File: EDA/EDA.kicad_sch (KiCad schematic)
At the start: 38 parts, among them J2 Screw_Terminal_01x02, M1 Motor_Servo, U1 PMCF8316A1VRGFR, U2 LM2596S-5, U3 LM2678S-5

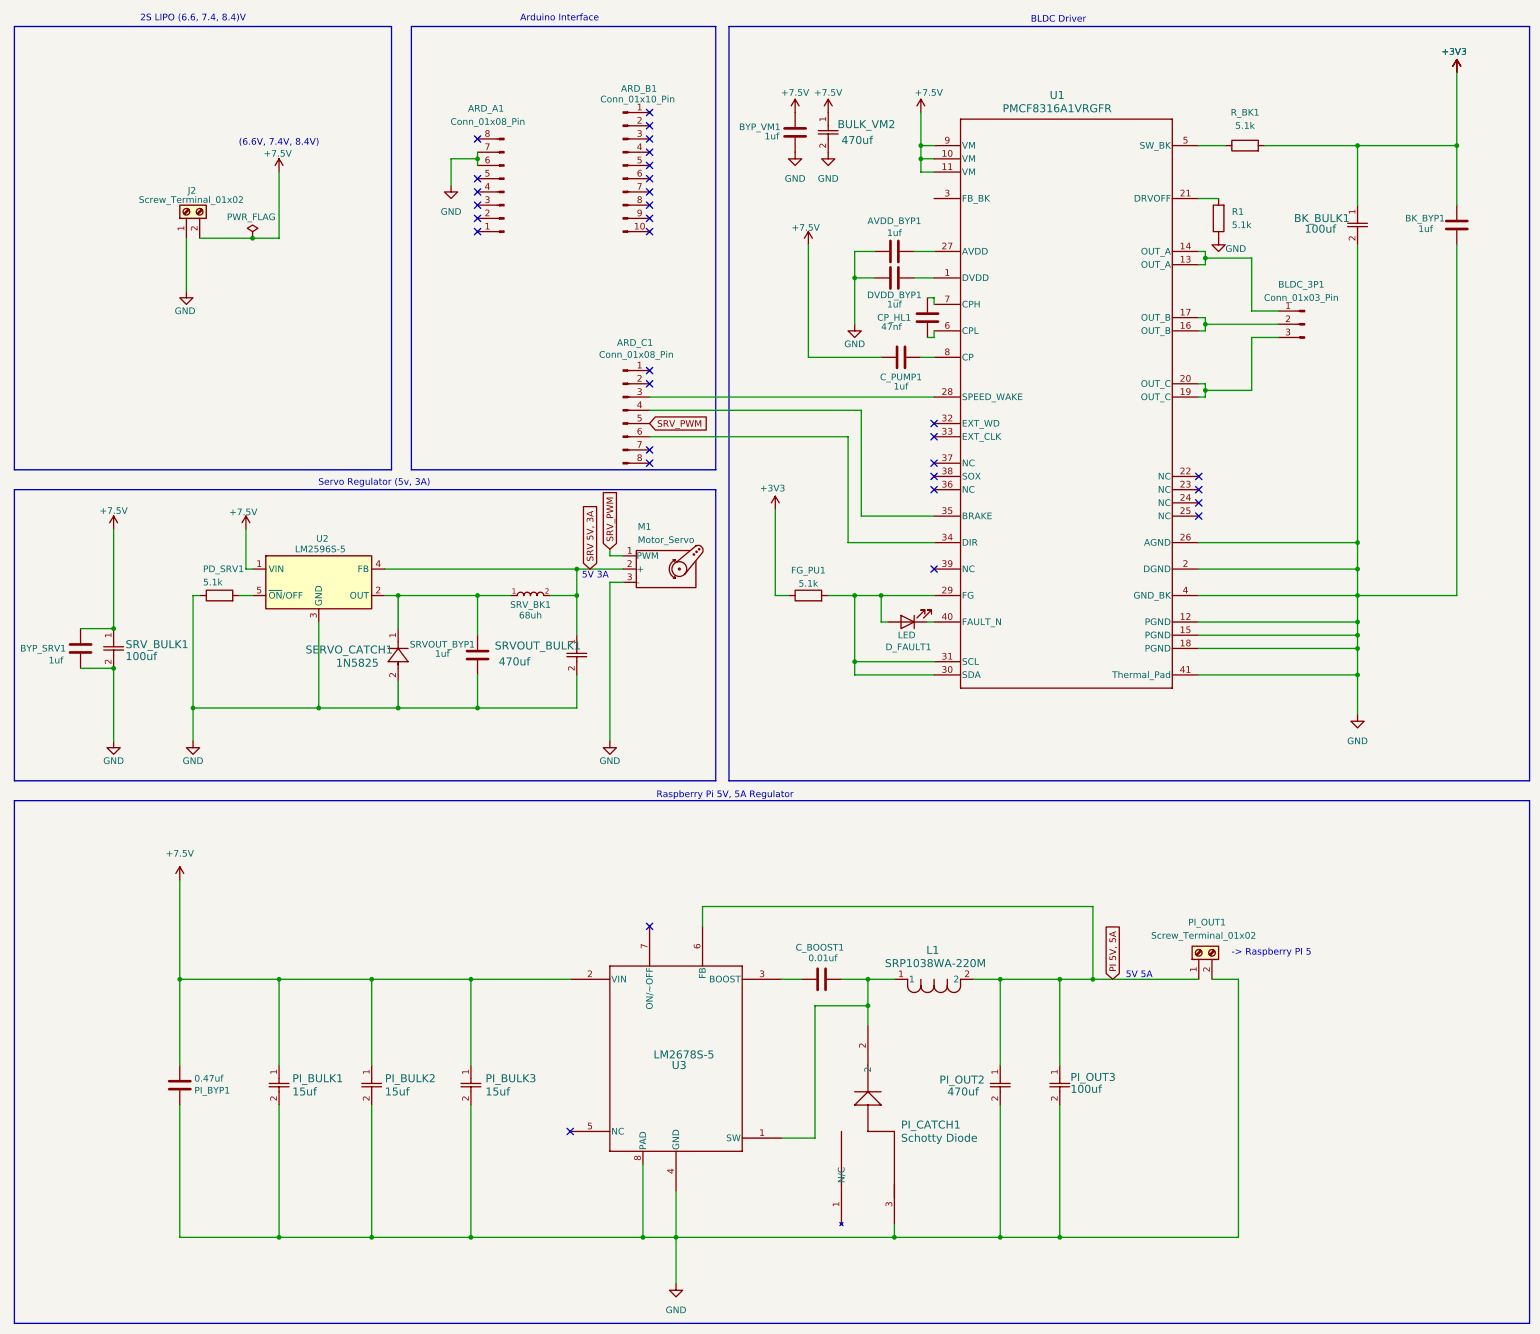
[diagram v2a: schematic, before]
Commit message: Add footprints for RGF0040E and LM2678S-12 components and update documentation
- Created new footprint files for RGF0040E-IPC_C and RGF0040E-MFG in KiCAD format.
- Created a new symbol for the LM2678S-12 in the KiCAD symbol library.
- Added three footprints (TS7B, TS7B-L, TS7B-M) for the LM2678S-12 in the KiCAD footprint library.
- Established a project plan document outlining milestones and tasks for upcoming development phases.
- Each footprint includes detailed pad and line definitions, along with silk screen and courtyard outlines.
- Updated properties for reference, value, and datasheet links in the symbol and footprints.
- Refactor schematic for clarity and readablity.
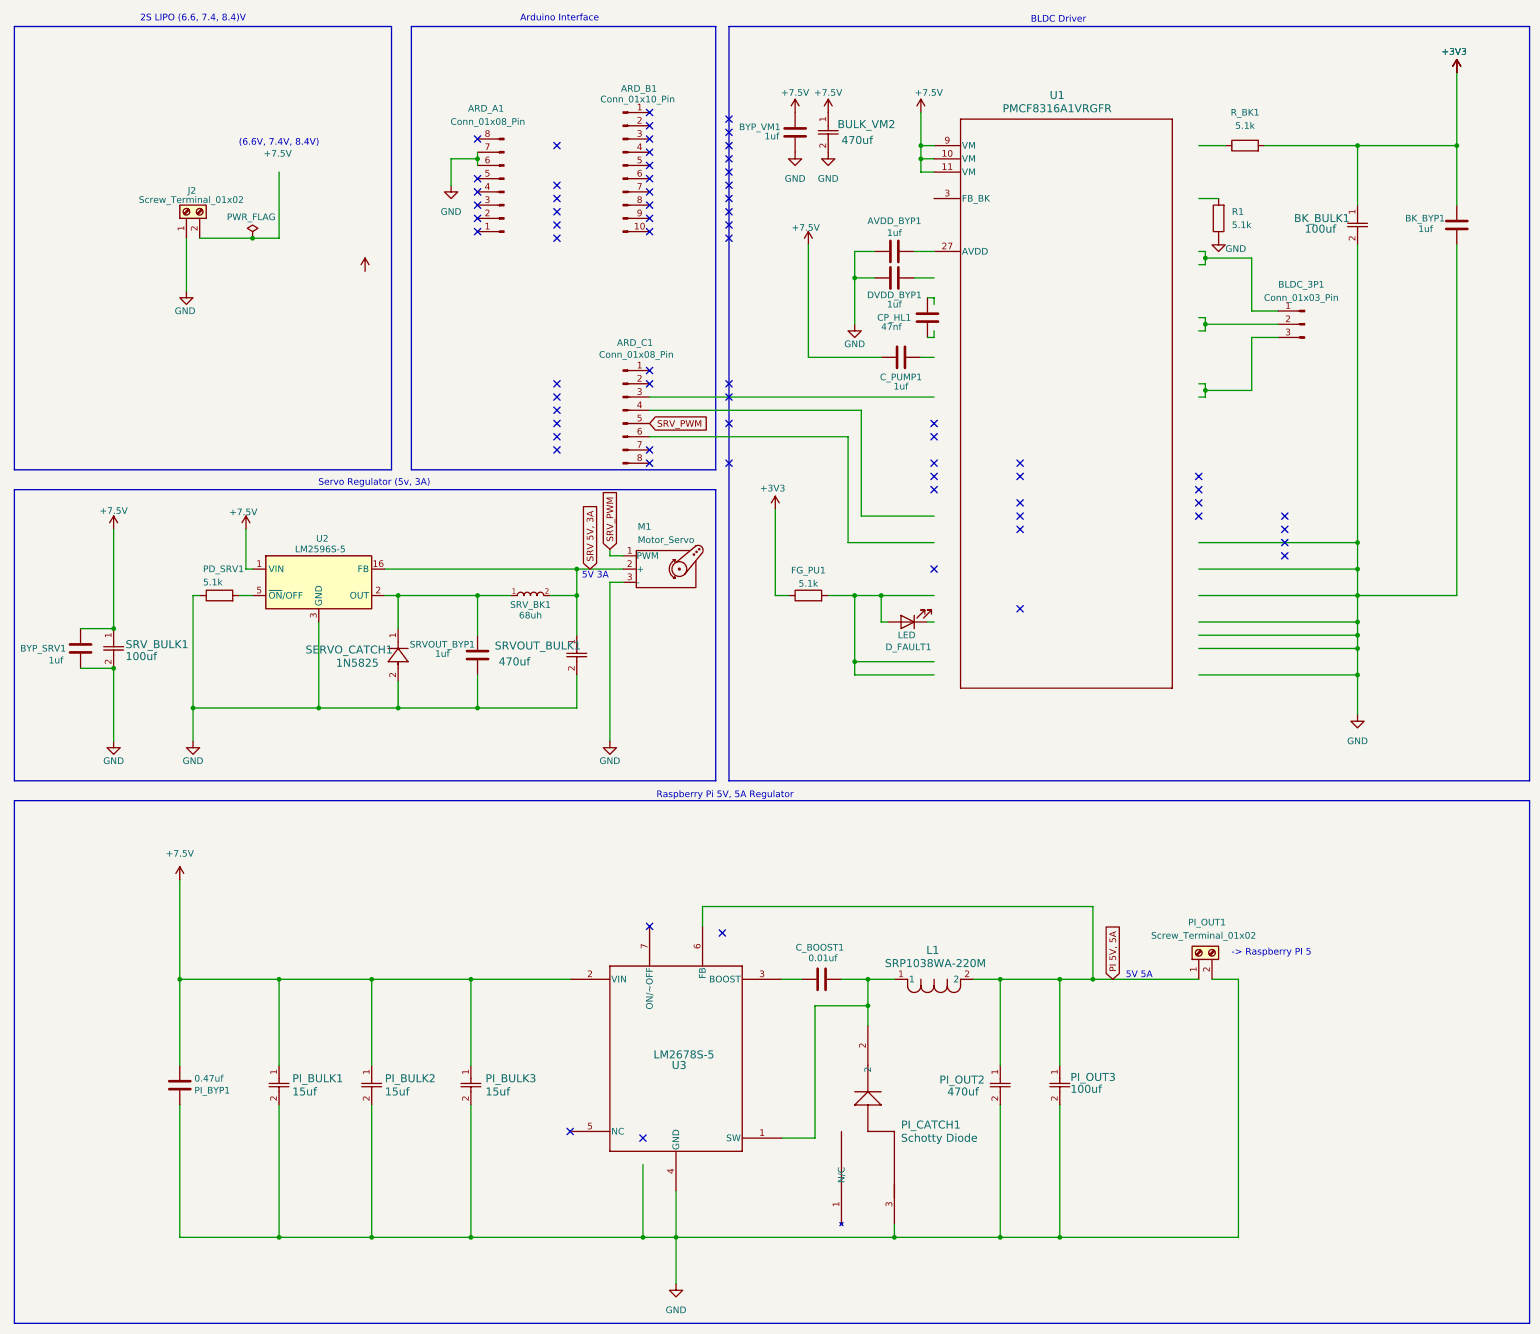
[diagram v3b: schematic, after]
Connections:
- net +7.5V: no longer J2.2 (Pin_2)
- net GND: no longer U1.12 (PGND), U1.15 (PGND), U1.18 (PGND), U1.2 (DGND), U1.26 (AGND), U1.4 (GND_BK), U1.41 (Thermal_Pad), U3.8 (PAD)
- net SRV 5V, 3A: now also U2.16 (FB); no longer U2.4 (FB)
- net at R_BK1.1: no longer U1.5 (SW_BK)
- net at ARD_C1.3 (Pin_3): no longer U1.28 (SPEED_WAKE)
- net at ARD_C1.4 (Pin_4): no longer U1.35 (BRAKE)
- net at ARD_C1.6 (Pin_6): no longer U1.34 (DIR)
- net at DVDD_BYP1.1: no longer U1.1 (DVDD)
- net at R1.2: no longer U1.21 (DRVOFF)
- net at D_FAULT1.1 (K): no longer U1.40 (FAULT_N)
- net at CP_HL1.2: no longer U1.6 (CPL)
- net at CP_HL1.1: no longer U1.7 (CPH)
- net at C_PUMP1.2: no longer U1.8 (CP)
- new net: D_FAULT1.2 (A), FG_PU1.2
- now unconnected: BLDC_3P1.1 (Pin_1), BLDC_3P1.2 (Pin_2), BLDC_3P1.3 (Pin_3)
- no-connect marks 32 -> 70
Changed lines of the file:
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@@
 		(at 105.41 38.1)
 	)
+	(no_connect
+		(at 153.67 41.91)
+	)
+	(no_connect
+		(at 260.35 115.57)
+	)
+	(no_connect
+		(at 152.4 190.5)
+	)
+	(no_connect
+		(at 153.67 34.29)
+	)
+	(no_connect
+		(at 209.55 113.03)
+	)
+	(no_connect
+		(at 209.55 102.87)
+	)
+	(no_connect
+		(at 153.67 49.53)
+	)
+	(no_connect
+		(at 153.67 39.37)
+	)
+	(no_connect
+		(at 120.65 52.07)
+	)
+	(no_connect
+		(at 137.16 229.87)
+	)
+	(no_connect
+		(at 153.67 87.63)
+	)
+	(no_connect
+		(at 209.55 128.27)
+	)
+	(no_connect
+		(at 120.65 87.63)
+	)
+	(no_connect
+		(at 120.65 95.25)
+	)
+	(no_connect
+		(at 153.67 85.09)
+	)
+	(no_connect
+		(at 120.65 97.79)
+	)
+	(no_connect
+		(at 153.67 100.33)
+	)
+	(no_connect
+		(at 260.35 118.11)
+	)
+	(no_connect
+		(at 120.65 46.99)
+	)
+	(no_connect
+		(at 153.67 54.61)
+	)
+	(no_connect
+		(at 153.67 36.83)
+	)
+	(no_connect
+		(at 153.67 44.45)
+	)
+	(no_connect
+		(at 260.35 110.49)
+	)
+	(no_connect
+		(at 120.65 57.15)
+	)
+	(no_connect
+		(at 153.67 46.99)
+	)
+	(no_connect
+		(at 120.65 49.53)
+	)
+	(no_connect
+		(at 209.55 100.33)
+	)
+	(no_connect
+		(at 153.67 52.07)
+	)
+	(no_connect
+		(at 209.55 110.49)
+	)
+	(no_connect
+		(at 120.65 39.37)
+	)
+	(no_connect
+		(at 120.65 54.61)
+	)
+	(no_connect
+		(at 120.65 92.71)
+	)
+	(no_connect
+		(at 120.65 90.17)
+	)
+	(no_connect
+		(at 120.65 85.09)
+	)
+	(no_connect
+		(at 153.67 92.71)
+	)
+	(no_connect
+		(at 153.67 57.15)
+	)
+	(no_connect
+		(at 260.35 113.03)
+	)
+	(no_connect
+		(at 209.55 107.95)
+	)
 	(wire
 		(pts
@@
 	(symbol
 		(lib_id "power:+7.5V")
-		(at 67.31 44.45 0)
+		(at 83.82 63.5 0)
 		(unit 1)
 		(exclude_from_sim no)
@@
 		(dnp no)
 		(property "Reference" "#PWR01"
-			(at 67.31 48.26 0)
+			(at 83.82 67.31 0)
 			(effects
 				(font
@@
 		)
 		(property "Footprint" ""
-			(at 67.31 44.45 0)
+			(at 83.82 63.5 0)
 			(effects
 				(font
@@
 		)
 		(property "Datasheet" ""
-			(at 67.31 44.45 0)
+			(at 83.82 63.5 0)
 			(effects
 				(font
@@
 		)
 		(property "Description" "Power symbol creates a global label with name \"+7.5V\""
-			(at 67.31 44.45 0)
+			(at 83.82 63.5 0)
 			(effects
 				(font
@@
 				(font
 					(size 1.27 1.27)
-					(italic yes)
 				)
 				(hide yes)
@@
 			)
 		)
+		(pin "2"
+		)
 		(pin "1"
